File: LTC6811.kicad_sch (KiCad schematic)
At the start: 2 parts, among them J1 Conn_01x13, U1 LTC6811-1

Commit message: Added part of power schematic
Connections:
- net V+: now reaches U1.1 (V+)
- net V-: now reaches U1.30 (V-), U1.31 (V-)
- net LTC_CS: now reaches U1.41 (CSB(IMA))
- net LTC_SCK: now reaches U1.42 (SCK(IPA))
- net LTC_SDI: now reaches U1.43 (SDI(NC))
- net LTC_SDO: now reaches U1.44 (SDO(NC))
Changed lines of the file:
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@@
+    (stroke (width 0) (type default) (color 0 0 0 0))
+  )
+  (wire (pts (xy 87.63 66.04) (xy 87.63 67.31))
     (stroke (width 0) (type default) (color 0 0 0 0))
   )
@@
     (stroke (width 0) (type default) (color 0 0 0 0))
   )
+  (wire (pts (xy 87.63 139.7) (xy 87.63 138.43))
+    (stroke (width 0) (type default) (color 0 0 0 0))
+  )
   (wire (pts (xy 100.33 80.01) (xy 105.41 80.01))
     (stroke (width 0) (type default) (color 0 0 0 0))
@@
     (effects (font (size 0.5 0.5)) (justify left bottom))
   )
+  (global_label "V-" (shape input) (at 87.63 139.7 270) (fields_autoplaced)
+    (effects (font (size 1.27 1.27)) (justify right))
+    (property "Intersheet References" "${INTERSHEET_REFS}" (id 0) (at 87.5506 144.7741 90)
+      (effects (font (size 1.27 1.27)) (justify right) hide)
+    )
+  )
+  (global_label "V+" (shape input) (at 87.63 66.04 90) (fields_autoplaced)
+    (effects (font (size 1.27 1.27)) (justify left))
+    (property "Intersheet References" "${INTERSHEET_REFS}" (id 0) (at 87.5506 60.9659 90)
+      (effects (font (size 1.27 1.27)) (justify left) hide)
+    )
+  )
+  (hierarchical_label "LTC_SDI" (shape input) (at 74.93 115.57 180)
+    (effects (font (size 1.27 1.27)) (justify right))
+  )
+  (hierarchical_label "LTC_SDO" (shape input) (at 74.93 118.11 180)
+    (effects (font (size 1.27 1.27)) (justify right))
+  )
+  (hierarchical_label "LTC_CS" (shape input) (at 74.93 110.49 180)
+    (effects (font (size 1.27 1.27)) (justify right))
+  )
+  (hierarchical_label "LTC_SCK" (shape input) (at 74.93 113.03 180)
+    (effects (font (size 1.27 1.27)) (justify right))
+  )
   (symbol (lib_id "Connector_Generic:Conn_01x13") (at 209.55 96.52 0) (unit 1)

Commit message: update
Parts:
- added R61, R62, R63, R64: 1M, symbol Device:R
- added TP2: CS, TestPoint:TestPoint_Pad_D1.5mm, symbol Connector:TestPoint
- added TP3: SCK, TestPoint:TestPoint_Pad_D1.5mm, symbol Connector:TestPoint
- added TP4: SDI, TestPoint:TestPoint_Pad_D1.5mm, symbol Connector:TestPoint
- added TP5: SDO, TestPoint:TestPoint_Pad_D1.5mm, symbol Connector:TestPoint
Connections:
- net LTC_CS: now also R61.2, TP2.1
- net LTC_SCK: now also R62.2, TP3.1
- net LTC_SDI: now also R63.2, TP4.1
- net LTC_SDO: now also R64.2, TP5.1
- new net +3V3: R61.1, R62.1, R63.1, R64.1

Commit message: routed most tracks
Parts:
- removed TP2: CS, TestPoint:TestPoint_Pad_D1.5mm, symbol Connector:TestPoint
- removed TP3: SCK, TestPoint:TestPoint_Pad_D1.5mm, symbol Connector:TestPoint
- removed TP4: SDI, TestPoint:TestPoint_Pad_D1.5mm, symbol Connector:TestPoint
- removed TP5: SDO, TestPoint:TestPoint_Pad_D1.5mm, symbol Connector:TestPoint
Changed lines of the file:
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@@
-    (stroke (width 0) (type default) (color 0 0 0 0))
-  )
-  (wire (pts (xy 63.5 127) (xy 63.5 115.57))
     (stroke (width 0) (type default) (color 0 0 0 0))
   )
@@
     (effects (font (size 1.27 1.27)) (justify right))
   )
-  (symbol (lib_id "Connector:TestPoint") (at 63.5 127 0) (unit 1)
-    (in_bom yes) (on_board yes)
-    (property "Reference" "TP4" (id 0) (at 62.23 121.92 0)
-      (effects (font (size 1.27 1.27)) (justify left))
-    )
-    (property "Value" "SDI" (id 1) (at 63.5 125.73 0)
-      (effects (font (size 1.27 1.27)) (justify left))
-    )
-    (property "Footprint" "TestPoint:TestPoint_Pad_D1.5mm" (id 2) (at 68.58 127 0)
-      (effects (font (size 1.27 1.27)) hide)
-    )
-    (property "Datasheet" "~" (id 3) (at 68.58 127 0)
-      (effects (font (size 1.27 1.27)) hide)
-    )
-    (pin "1")
-  )
   (symbol (lib_id "Device:R") (at 53.34 99.06 0) (unit 1)
     (in_bom yes) (on_board yes) (fields_autoplaced)
@@
     (pin "1")
     (pin "2")
-  )
-  (symbol (lib_id "Connector:TestPoint") (at 68.58 127 0) (unit 1)
-    (in_bom yes) (on_board yes)
-    (property "Reference" "TP5" (id 0) (at 67.31 121.92 0)
-      (effects (font (size 1.27 1.27)) (justify left))
-    )
-    (property "Value" "SDO" (id 1) (at 68.58 125.73 0)
-      (effects (font (size 1.27 1.27)) (justify left))
-    )
-    (property "Footprint" "TestPoint:TestPoint_Pad_D1.5mm" (id 2) (at 73.66 127 0)
-      (effects (font (size 1.27 1.27)) hide)
-    )
-    (property "Datasheet" "~" (id 3) (at 73.66 127 0)
-      (effects (font (size 1.27 1.27)) hide)
-    )
-    (pin "1")
   )
   (symbol (lib_id "Device:R") (at 68.58 99.06 0) (unit 1)
@@
     (pin "9")
   )
-  (symbol (lib_id "Connector:TestPoint") (at 53.34 127 0) (unit 1)
-    (in_bom yes) (on_board yes)
-    (property "Reference" "TP2" (id 0) (at 52.07 121.92 0)
-      (effects (font (size 1.27 1.27)) (justify left))
-    )
-    (property "Value" "CS" (id 1) (at 53.34 125.73 0)
-      (effects (font (size 1.27 1.27)) (justify left))
-    )
-    (property "Footprint" "TestPoint:TestPoint_Pad_D1.5mm" (id 2) (at 58.42 127 0)
-      (effects (font (size 1.27 1.27)) hide)
-    )
-    (property "Datasheet" "~" (id 3) (at 58.42 127 0)
-      (effects (font (size 1.27 1.27)) hide)
-    )
-    (pin "1")
-  )
-  (symbol (lib_id "Connector:TestPoint") (at 58.42 127 0) (unit 1)
-    (in_bom yes) (on_board yes)
-    (property "Reference" "TP3" (id 0) (at 57.15 121.92 0)
-      (effects (font (size 1.27 1.27)) (justify left))
-    )
-    (property "Value" "SCK" (id 1) (at 58.42 125.73 0)
-      (effects (font (size 1.27 1.27)) (justify left))
-    )
-    (property "Footprint" "TestPoint:TestPoint_Pad_D1.5mm" (id 2) (at 63.5 127 0)
-      (effects (font (size 1.27 1.27)) hide)
-    )
-    (property "Datasheet" "~" (id 3) (at 63.5 127 0)
-      (effects (font (size 1.27 1.27)) hide)
-    )
-    (pin "1")
-  )
   (symbol (lib_id "power:+3V3") (at 53.34 90.17 0) (unit 1)

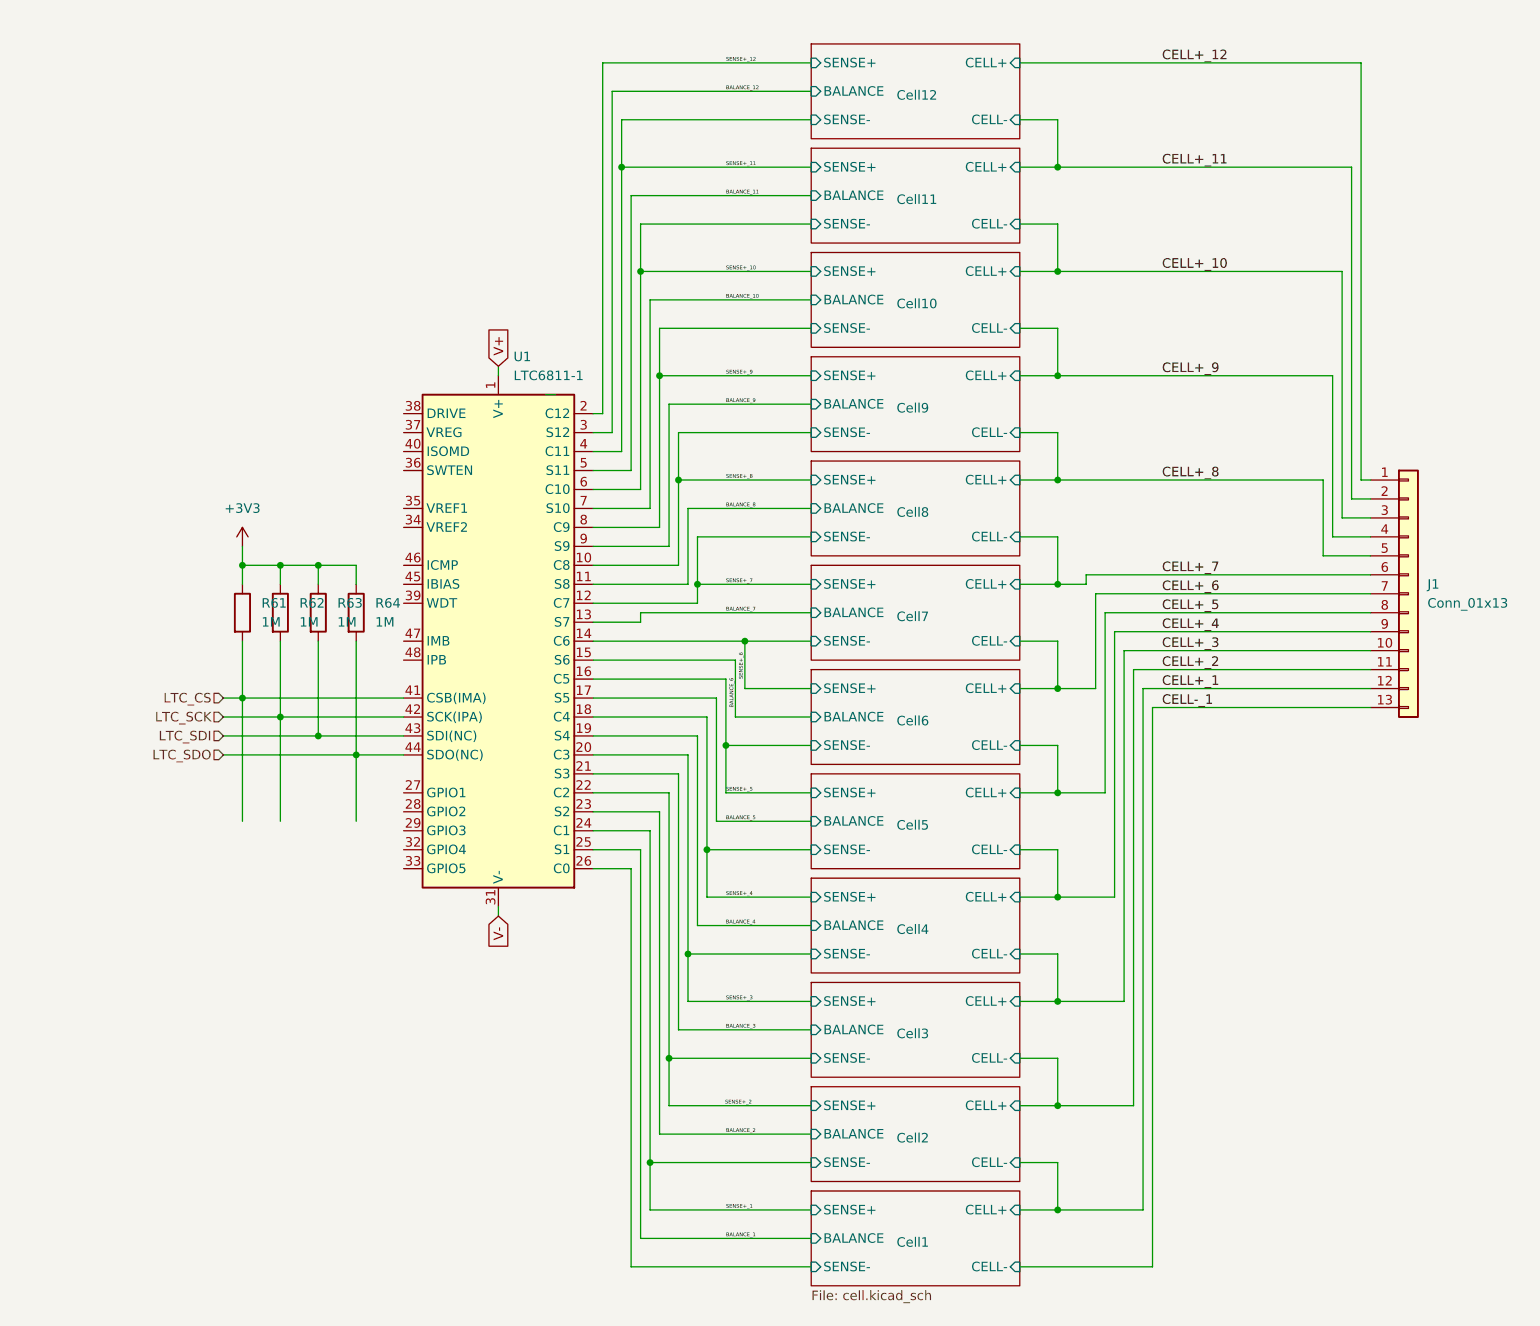
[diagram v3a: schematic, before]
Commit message: new board dimensions
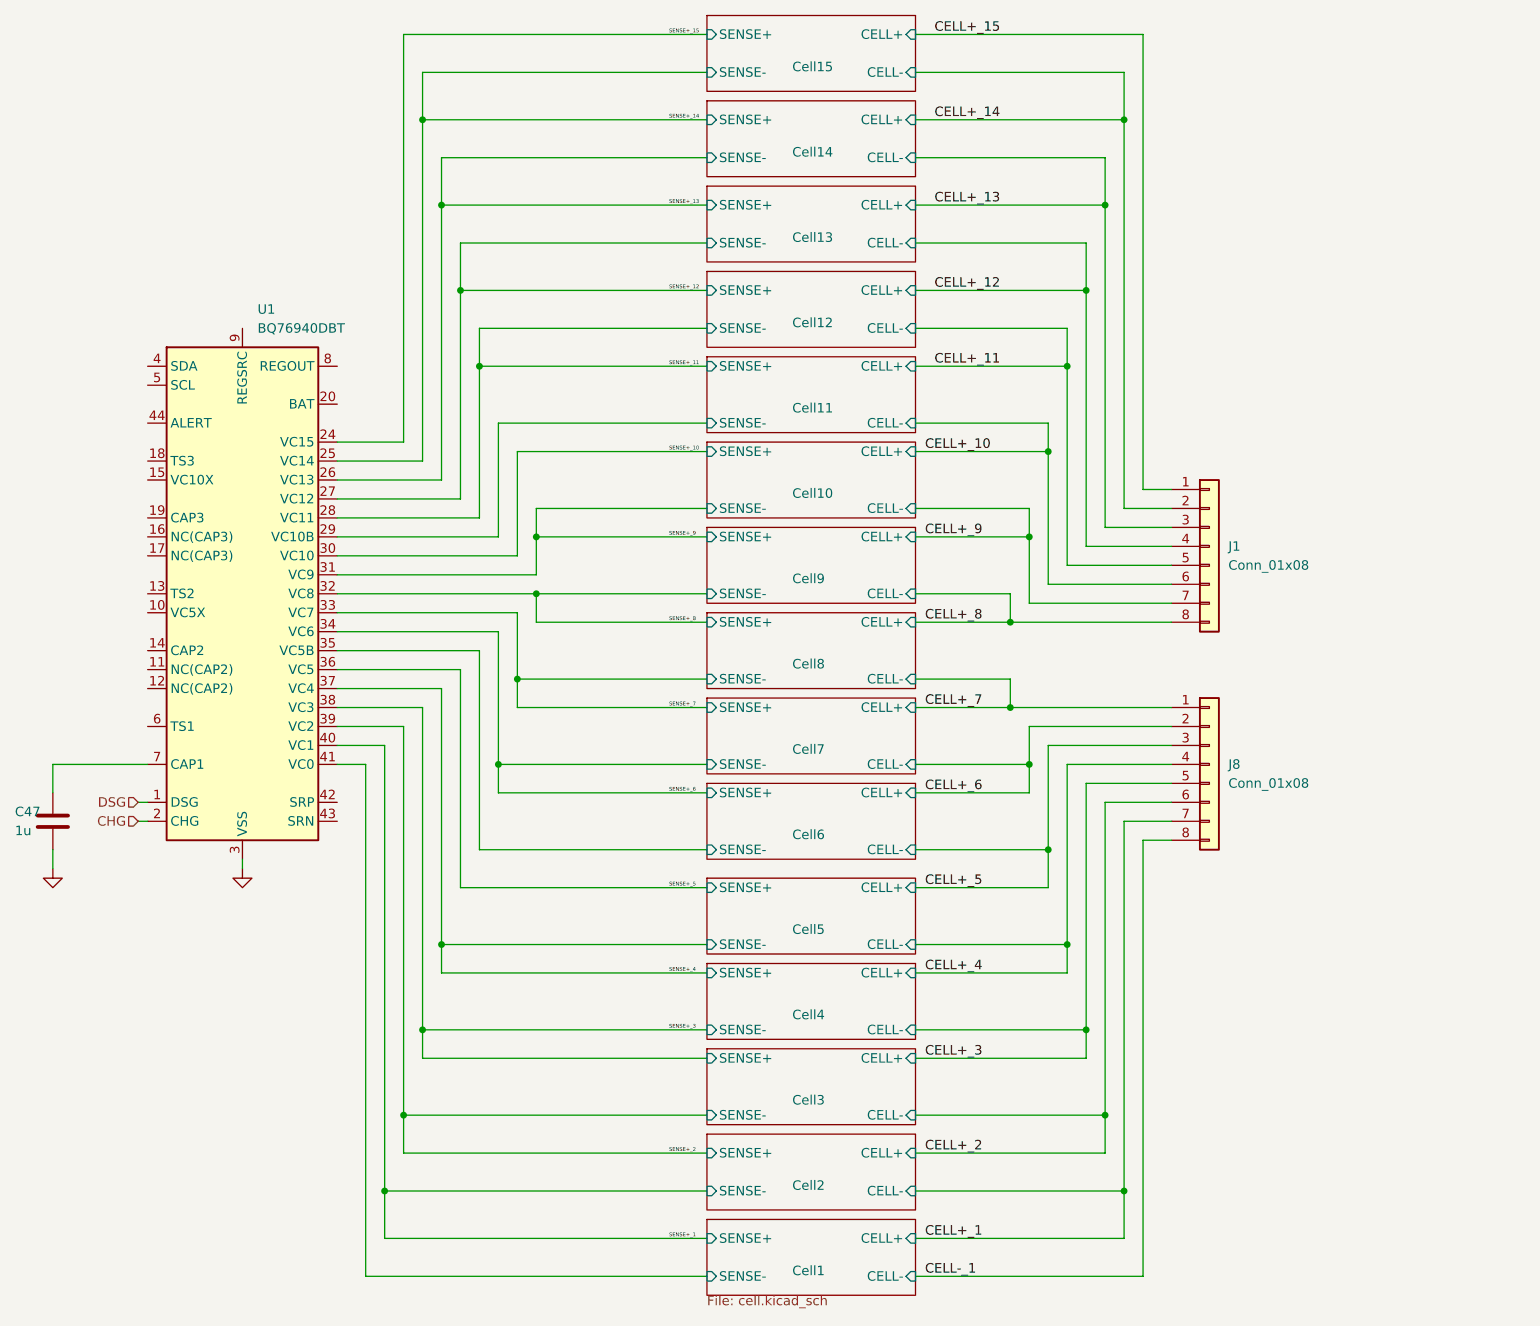
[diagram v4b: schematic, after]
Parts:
- removed J1: Conn_01x13, Connector_JST:JST_XH_B13B-XH-A_1x13_P2.50mm_Vertical, symbol Connector_Generic:Conn_01x13
- removed R61, R62, R63, R64: 1M, symbol Device:R
- removed U1: LTC6811-1, Package_SO:SSOP-48_5.3x12.8mm_P0.5mm, symbol Battery_Management:LTC6804-1
- added C47: 1u, symbol Device:C
- added J1, J8: Conn_01x08, Connector_JST:JST_XH_B8B-XH-A_1x08_P2.50mm_Vertical, symbol Connector_Generic:Conn_01x08
- added U1: BQ76940DBT, Package_SO:TSSOP-44_4.4x11.2mm_P0.5mm, symbol Battery_Management:BQ76940DBT
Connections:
- net CELL+_1: now also J8.7 (Pin_7)
- net CELL+_10: now also J1.6 (Pin_6)
- net CELL+_11: now also J1.5 (Pin_5)
- net CELL+_12: now also J1.4 (Pin_4)
- net CELL+_2: now also J8.6 (Pin_6)
- net CELL+_3: now also J8.5 (Pin_5)
- net CELL+_4: now also J8.4 (Pin_4)
- net CELL+_5: now also J8.3 (Pin_3)
- net CELL+_6: now also J8.2 (Pin_2)
- net CELL+_7: now also J8.1 (Pin_1)
- net CELL+_8: now also J1.8 (Pin_8)
- net CELL+_9: now also J1.7 (Pin_7)
- net CELL-_1: now also J8.8 (Pin_8)
- net Cell1/SENSE-: now also U1.41 (VC0)
- net SENSE+_1: now also U1.40 (VC1)
- net SENSE+_10: now also U1.30 (VC10)
- net SENSE+_11: now also U1.28 (VC11)
- net SENSE+_12: now also U1.27 (VC12)
- net SENSE+_2: now also U1.39 (VC2)
- net SENSE+_3: now also U1.38 (VC3)
- net SENSE+_4: now also U1.37 (VC4)
- net SENSE+_5: now also U1.36 (VC5)
- net SENSE+_6: now also U1.34 (VC6)
- net SENSE+_7: now also U1.33 (VC7)
- net SENSE+_8: now also U1.32 (VC8)
- net SENSE+_9: now also U1.31 (VC9)
- new net: C47.1, U1.7 (CAP1)
- new net CELL+_13: J1.3 (Pin_3)
- new net CELL+_14: J1.2 (Pin_2)
- new net CELL+_15: J1.1 (Pin_1)
- new net CHG: U1.2 (CHG)
- new net Cell11/SENSE-: U1.29 (VC10B)
- new net Cell6/SENSE-: U1.35 (VC5B)
- new net DSG: U1.1 (DSG)
- new net GND: C47.2, U1.3 (VSS)
- new net SENSE+_13: U1.26 (VC13)
- new net SENSE+_14: U1.25 (VC14)
- new net SENSE+_15: U1.24 (VC15)
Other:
- added sheet Cell13 (cell.kicad_sch)
- added sheet Cell14 (cell.kicad_sch)
- added sheet Cell15 (cell.kicad_sch)
- sheet Cell1 ports: added none; removed BALANCE
- sheet Cell10 ports: added none; removed BALANCE
- sheet Cell11 ports: added none; removed BALANCE
- sheet Cell12 ports: added none; removed BALANCE
- sheet Cell2 ports: added none; removed BALANCE
- sheet Cell3 ports: added none; removed BALANCE
- sheet Cell4 ports: added none; removed BALANCE
- sheet Cell5 ports: added none; removed BALANCE
- sheet Cell6 ports: added none; removed BALANCE
- sheet Cell7 ports: added none; removed BALANCE
- sheet Cell8 ports: added none; removed BALANCE
- sheet Cell9 ports: added none; removed BALANCE
